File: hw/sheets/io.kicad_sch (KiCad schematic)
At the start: 21 parts, among them J2 TYPE-C-31-M-12, J3 TE_292303-7, J4 Hirose_DM3D-SF, J5 Wuerth_694106301002, J6 AudioJack4_Ground, J7 SFW15R-2STE1LF, J8 SFW15R-2STE1LF, J9 TYPE-C-31-M-12, Q1 AO3401A, Q2 AO3401A

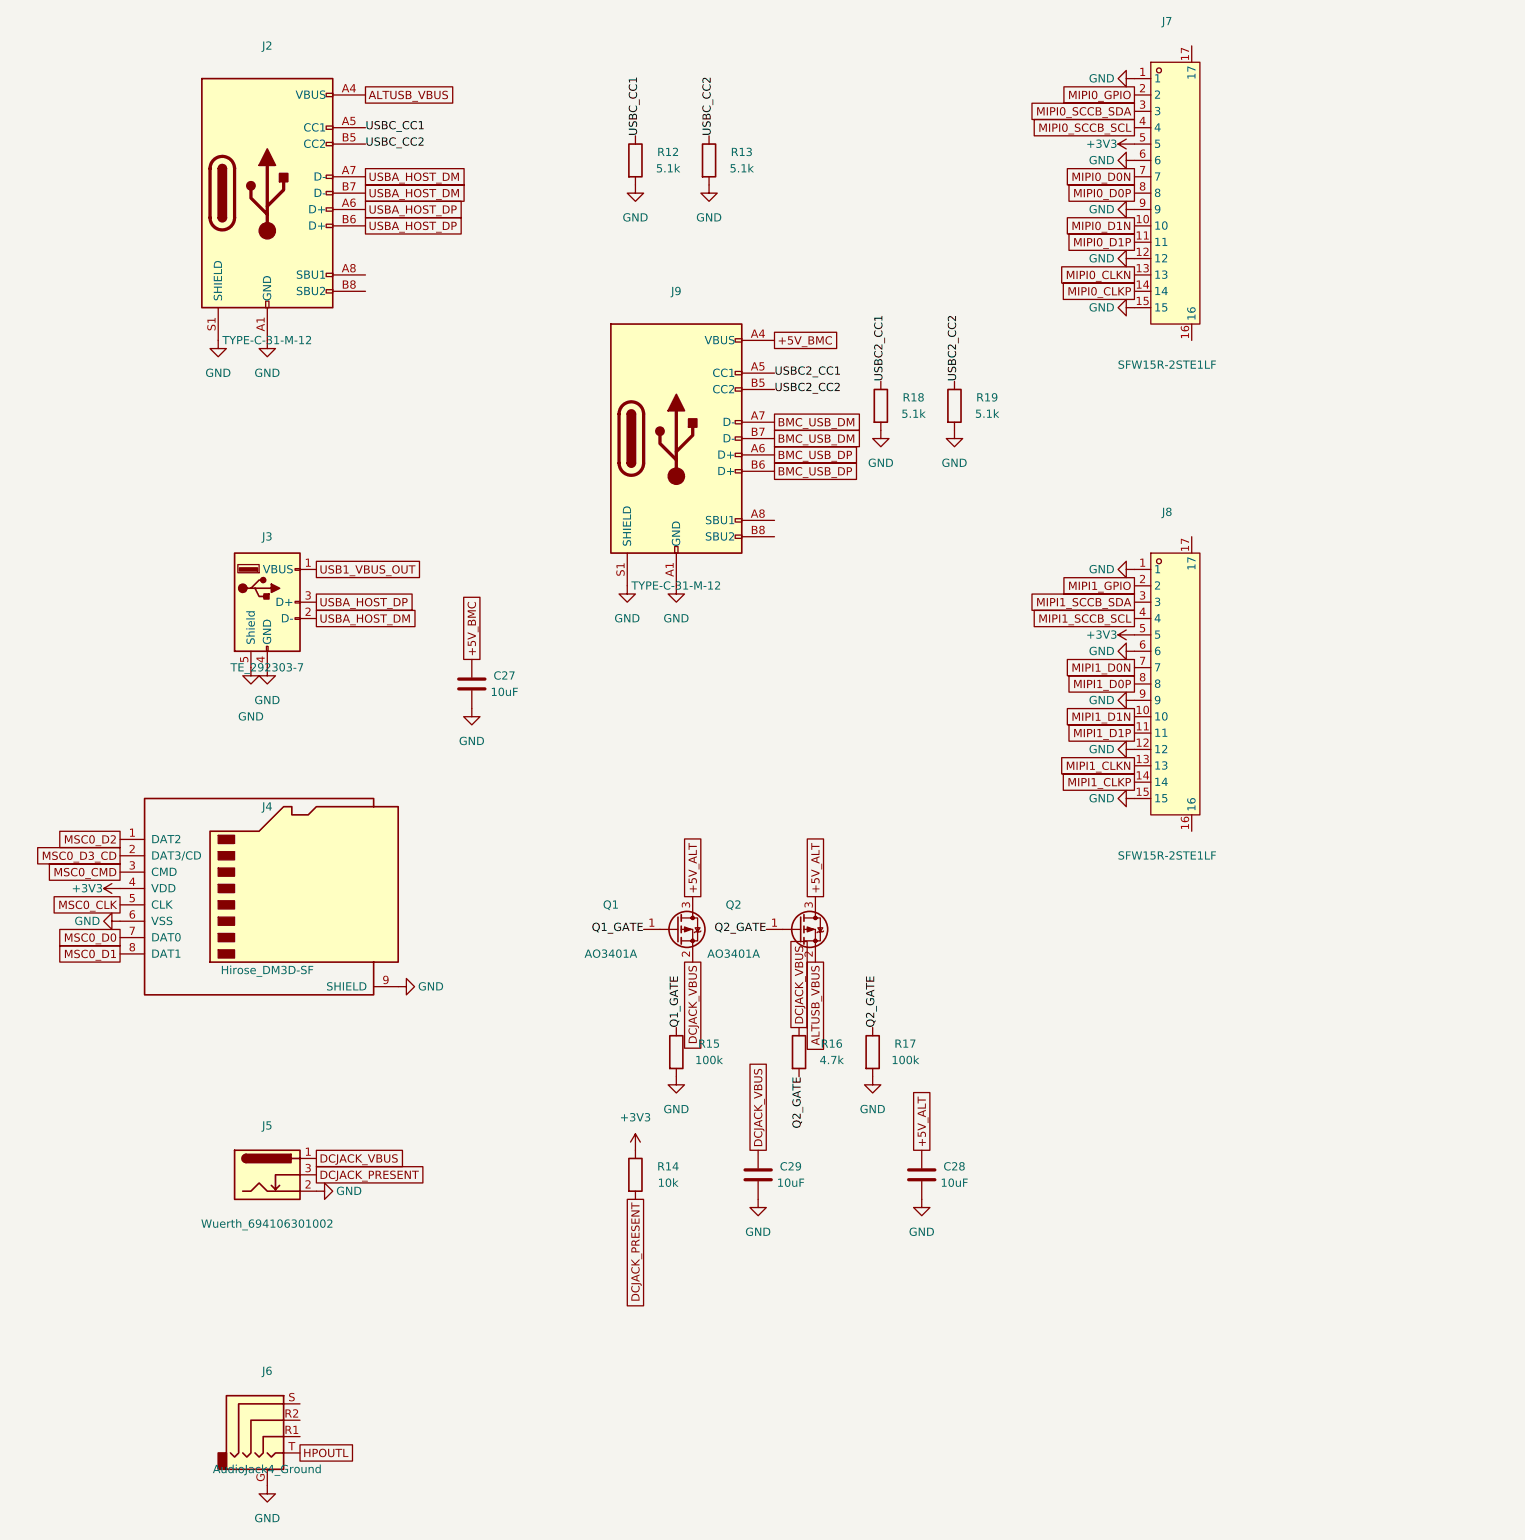
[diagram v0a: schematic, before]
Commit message: Carrier board: audio/FPC pinout fixes matching 3.3, SW2 remap, UART1 breakout, real PCB layout
Schematic fixes (verified pin-for-pin against TeaCup(C)3.3's real netlist,
not assumed):
- J6 audio jack: R1/R2 -> HPOUTL/GND, S -> MICLP, matching 3.3's J10 exactly
  (previous wiring incorrectly tied GND to a schematic pin, G, with no
  matching pad on the real Jack_3.5mm_PJ320D_Horizontal footprint).
- J7/J8 FPC camera connectors: full pin-for-pin remap to match 3.3's real
  J13 pinout -- the previous "standard RPi/Arducam" pinout had power/ground
  swapped, clock/data lanes in the wrong order, and reversed differential
  polarity throughout. Added JP11/JP12 sensor-enable select jumpers
  (GPIO vs hardwired +3V3), replicating 3.3's J15.
- J1 MIPI0/MIPI1 pin order on the connector reordered (CLK/D1/D0, P-before-N)
  to match J7/J8's now-fixed order, so routing between them doesn't need to
  cross over itself.
- HPOUTL relocated from J1 pin 58 (isolated, far from any other audio net)
  down to sit beside MICLP at pins 170-172, geography-first per
  UNIVERSAL.md SS8.
- SW2 (manual power-override switch) throw1/throw4 swapped: throw1 now
  forces ALT, throw4 now forces BMC.
- New J36 header breaks out UART1 (the BMC-ESP32<->J1 console link) for
  external monitoring, same as UART0/2/3 already had.

All verified via isolated before/after ERC diffs -- each change nets to
either 0 or a fully-explained delta against the 429-violation baseline,
never an unexplained regression.

PCB: teacup-carrier.kicad_pcb replaced with the manually-laid-out board
(previously developed as a separate merge-test attempt): real component
placement grouped by circuit block, board outline resized twice to
snugly enclose the layout, GND copper pour on both F.Cu and B.Cu, and
mounting holes repositioned to match. The old rough auto-placed board is
gone.
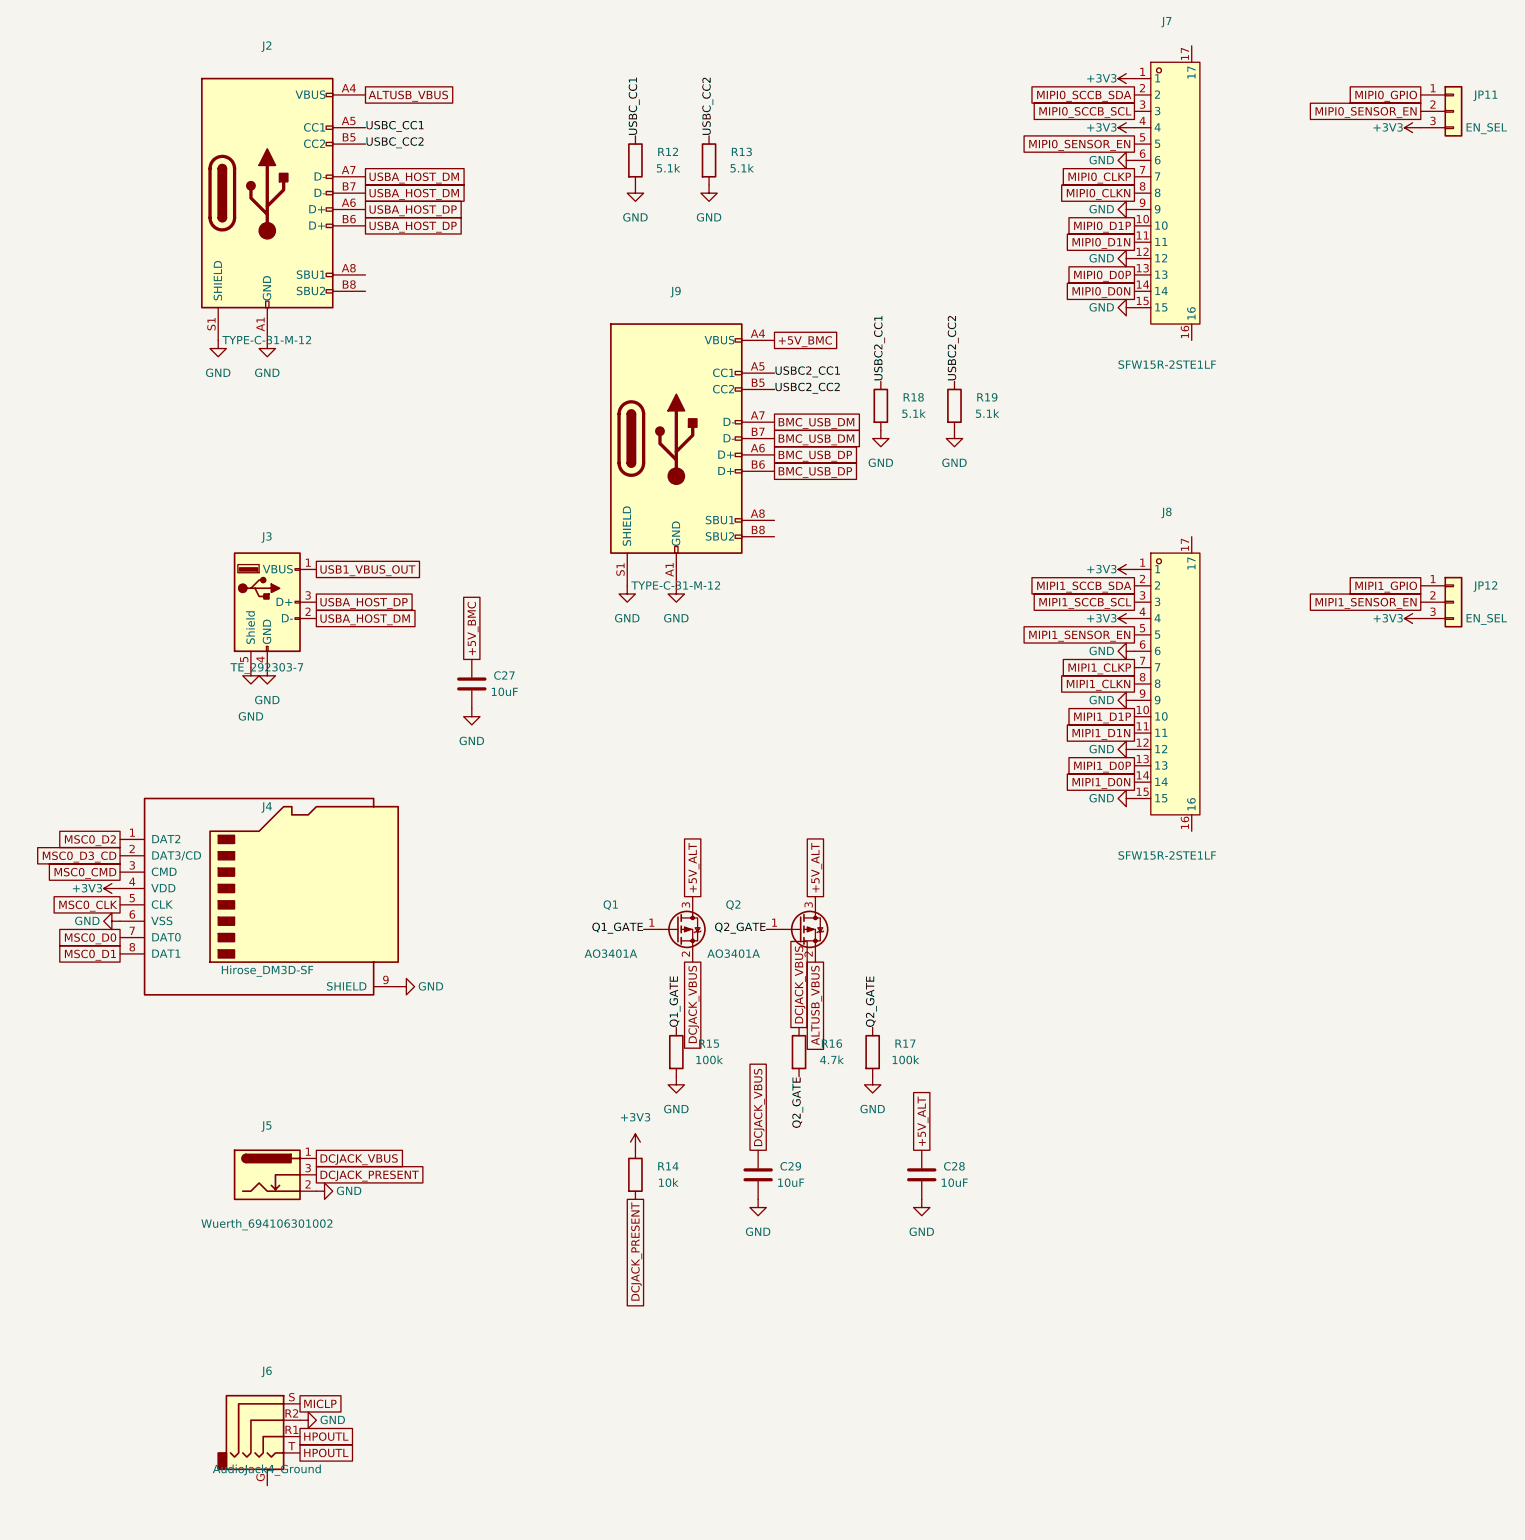
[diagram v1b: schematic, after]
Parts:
- added JP11, JP12: EN_SEL, Connector_PinHeader_2.54mm:PinHeader_1x03_P2.54mm_Vertical_SMD_Pin1Left, symbol Connector_Generic:Conn_01x03
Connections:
- net +3V3: now also J7.1, J7.4, J8.1, J8.4, JP11.3 (Pin_3), JP12.3 (Pin_3); no longer J7.5, J8.5
- net GND: now also J6.R2; no longer J6.G, J7.1, J8.1
- net HPOUTL: now also J6.R1
- net MIPI0_CLKN: now also J7.8; no longer J7.13
- net MIPI0_CLKP: now also J7.7; no longer J7.14
- net MIPI0_D0N: now also J7.14; no longer J7.7
- net MIPI0_D0P: now also J7.13; no longer J7.8
- net MIPI0_D1N: now also J7.11; no longer J7.10
- net MIPI0_D1P: now also J7.10; no longer J7.11
- net MIPI0_GPIO: now also JP11.1 (Pin_1); no longer J7.2
- net MIPI0_SCCB_SCL: now also J7.3; no longer J7.4
- net MIPI0_SCCB_SDA: now also J7.2; no longer J7.3
- net MIPI1_CLKN: now also J8.8; no longer J8.13
- net MIPI1_CLKP: now also J8.7; no longer J8.14
- net MIPI1_D0N: now also J8.14; no longer J8.7
- net MIPI1_D0P: now also J8.13; no longer J8.8
- net MIPI1_D1N: now also J8.11; no longer J8.10
- net MIPI1_D1P: now also J8.10; no longer J8.11
- net MIPI1_GPIO: now also JP12.1 (Pin_1); no longer J8.2
- net MIPI1_SCCB_SCL: now also J8.3; no longer J8.4
- net MIPI1_SCCB_SDA: now also J8.2; no longer J8.3
- net MICLP: now reaches J6.S
- new net MIPI0_SENSOR_EN: J7.5, JP11.2 (Pin_2)
- new net MIPI1_SENSOR_EN: J8.5, JP12.2 (Pin_2)
